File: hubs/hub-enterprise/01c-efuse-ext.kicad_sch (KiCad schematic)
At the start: 12 parts, among them J103 PJ-002AH, U103 TPS25940LRVCR

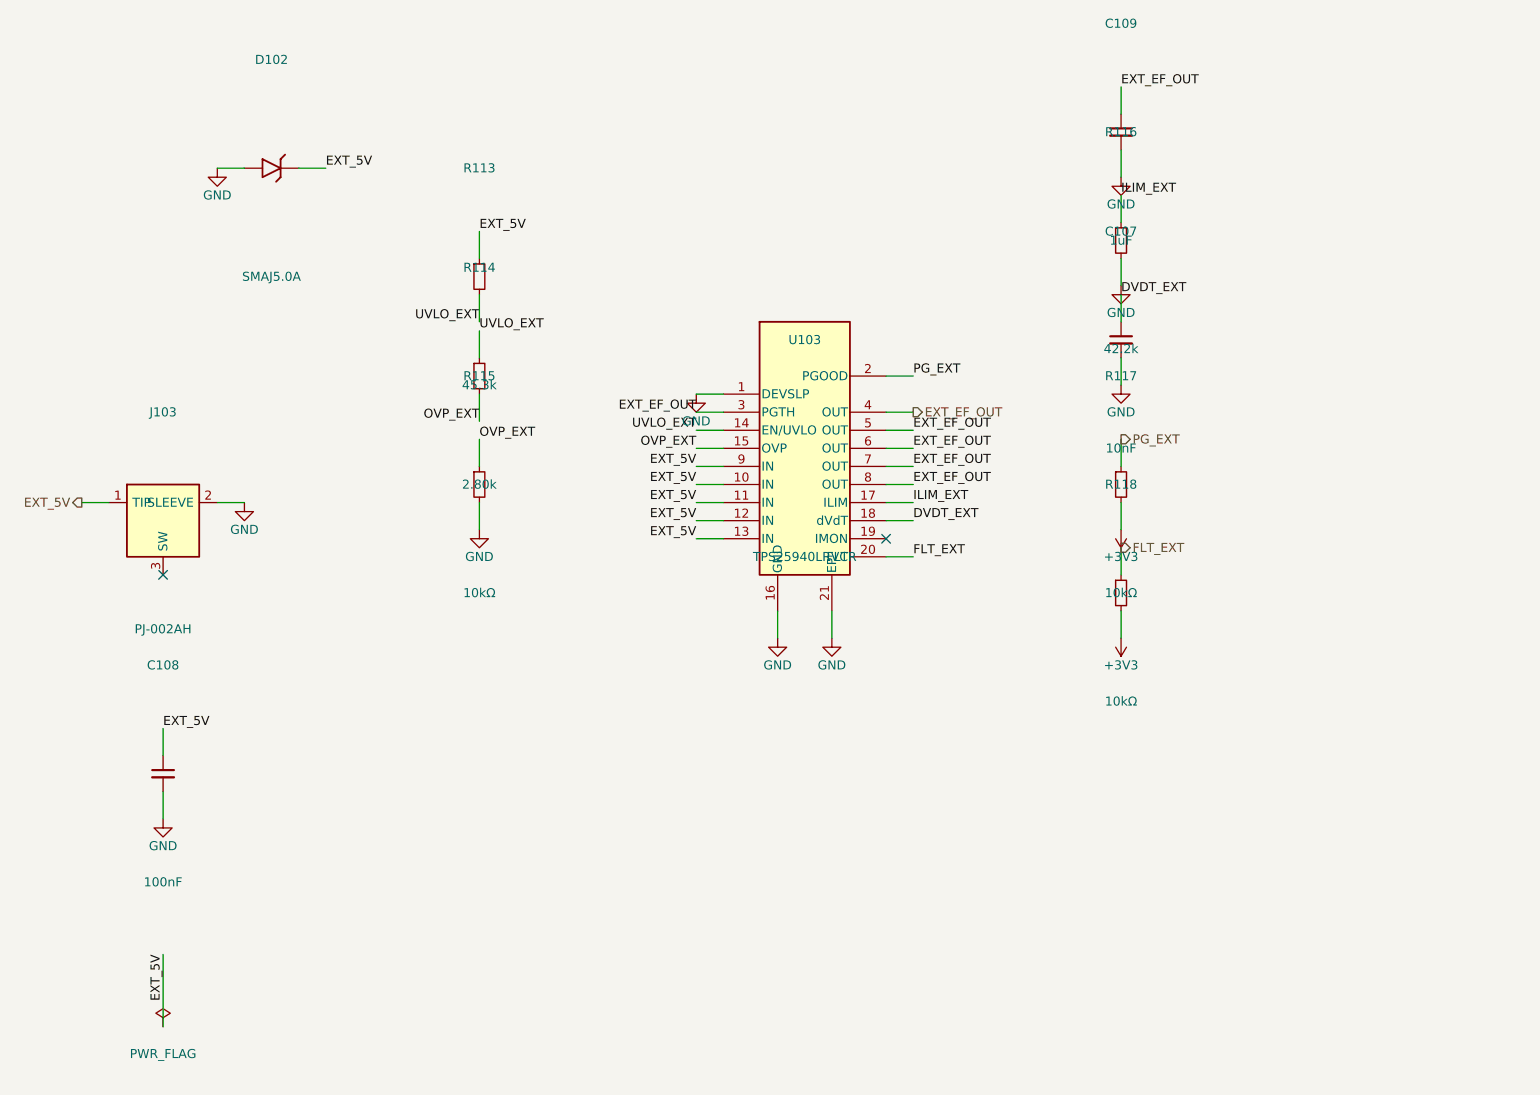
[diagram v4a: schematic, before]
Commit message: T1 composition pass: centered sheets, wired decouplers, drawn structure
Owner ask applied across the generated ENT hub sheets: content is
centered on the page (leaves moved A3->A4), decoupling caps sit at
their owner IC and connect by real drawn Manhattan wires instead of
floating label aliases, divider chains / pull-ups / ILIM parts are
drawn structure, and the thin parent is a genuine flow diagram --
per-side sheet pins, real eFuse->cascade fan-in wires on collision-free
lanes, EXT_5V routed to rail-sense with a junctioned tap, sheet-pin
names rendered inside their boxes (the owner-visible garble was the
justify convention, measured and fixed).

Mechanisms: build_leaf consumes a composed layout (wires, hier_at
overrides, decoupler rails, per-part text side) with a content-bbox
centering pass, geometry-aware Ref/Value placement, auto-junctions,
and away-side power stamps; per-leaf compose_*() in the generator (one
eFuse template drives 01a/b/c; 01e runs place_decouplers/
wire_decouplers verbatim); nudge_texts as the finishing pass. The
parent's box geometry is grid-aligned so sheet pins sit both on-edge
and on-grid -- the entire endpoint_off_grid ERC class is gone (19->0).

Real T1 bug found via render iteration: property bboxes must be
computed at the RENDERED angle (symbol rotation + field angle) -- a
rot-90 inductor's value was bboxed vertical, false-collided, and got
nudged 40mm away. Fixed in cec_sch_layout with RotatedFieldBBoxTest
(12/12).

Gates, all verified independently: netlist identity 0 missing/0 extra
(59 components, 46 groups, checker exit 0); ERC 4 benign classes only,
no annotation warning; overlaps 0 on all 8 generated sheets (was 45
pairs); lint ERROR 0 (was 38), 15 documented SL-04 WARNs. Charter T1
row: integration DONE; gates 5/6 ADOPTED into the per-sheet protocol.

Co-Authored-By: Claude Fable 5 <noreply@anthropic.com>
Claude-Session: https://claude.ai/code/session_011q5bmwF5BFtSf8Ft5vT1DZ
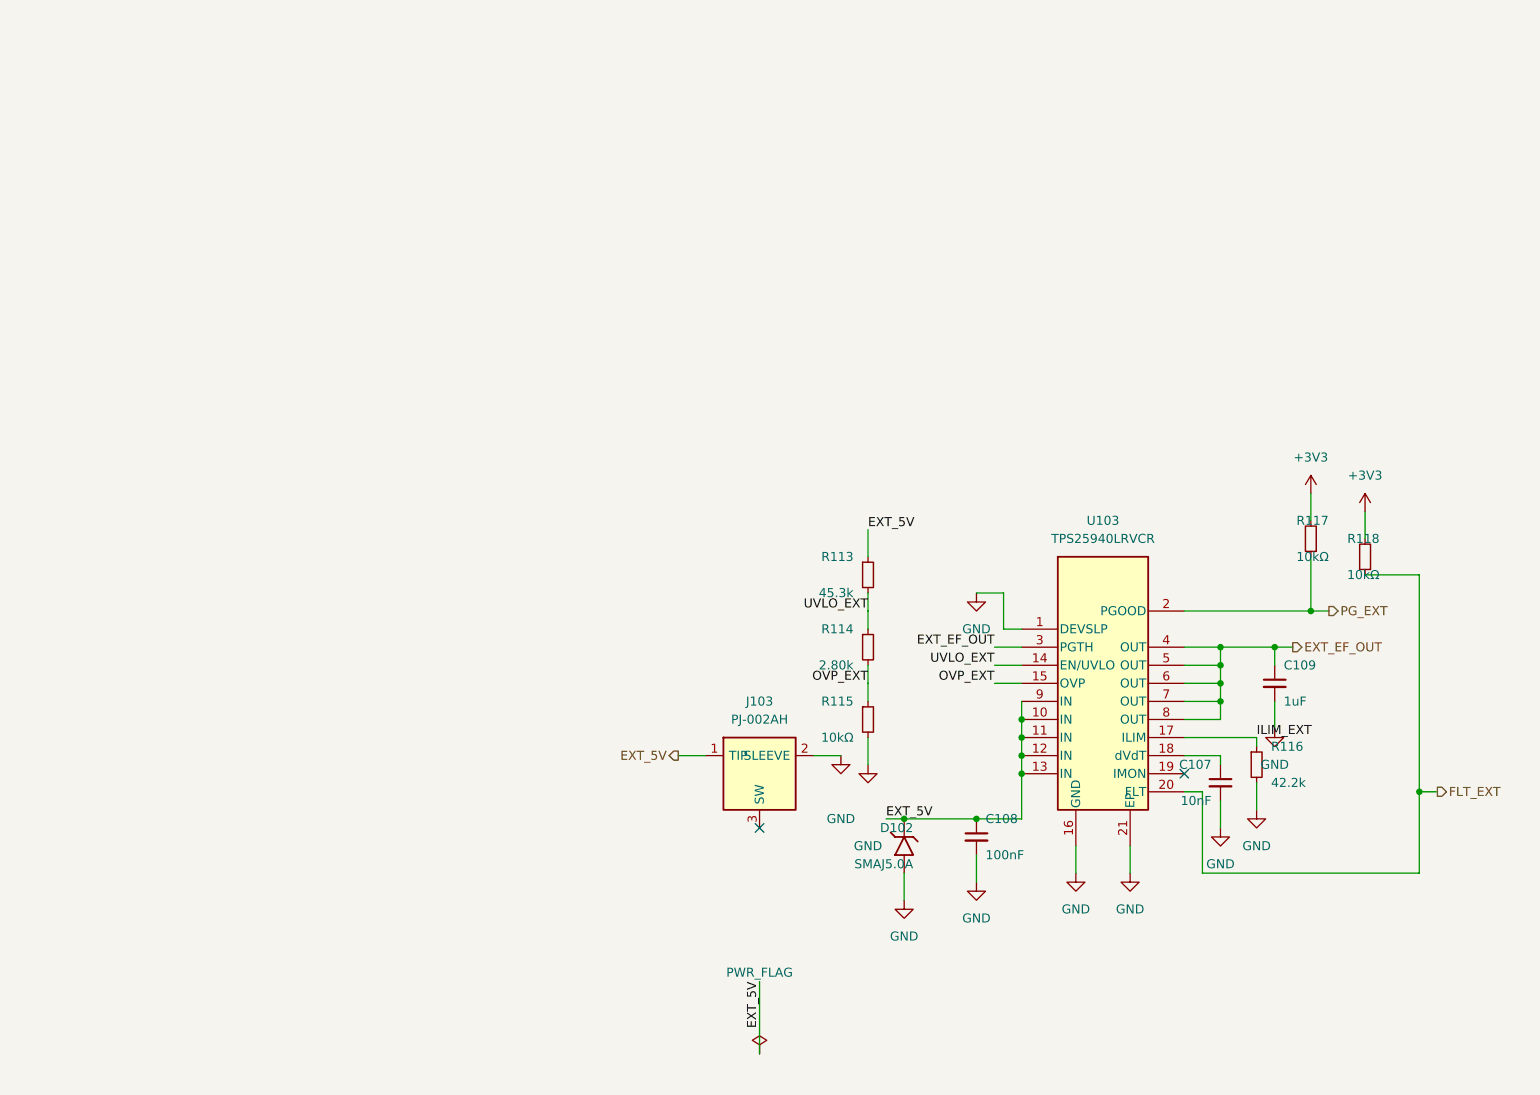
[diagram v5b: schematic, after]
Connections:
- net DVDT_EXT: no longer names the net of C107.1, U103.18 (dVdT)

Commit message: WIP snapshot: composition agent hub regeneration in flight (durability)
Co-Authored-By: Claude Fable 5 <noreply@anthropic.com>
Claude-Session: https://claude.ai/code/session_011q5bmwF5BFtSf8Ft5vT1DZ
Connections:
- net EXT_5V is gone; now on net GND: C108.1, D102.2 (K), J103.1 (TIP), R113.1, U103.10 (IN), U103.11 (IN), U103.12 (IN), U103.13 (IN), U103.9 (IN)
- net FLT_EXT: now also R118.2
- net PG_EXT: now also R117.2
- removed net +3V3: R117.2, R118.2
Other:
- note added: "EXT eFuse front + TVS (TPS25940, ILIM 42.2k -> 2.08A typ, SMAJ5.0A + PJ-002AH)"
- note added: "SMAJ5.0A input TVS populated on EXT only (mirrors the DETECT-pin philosophy); PJ-002AH barrel jack per BOM-D"
- note added: "UVLO/OVLO divider 45.3k/2.80k/10k -> 4.49V UV / 5.75V OV; ILIM 42.2k -> 2.08A typ (bom-d-power.md)"

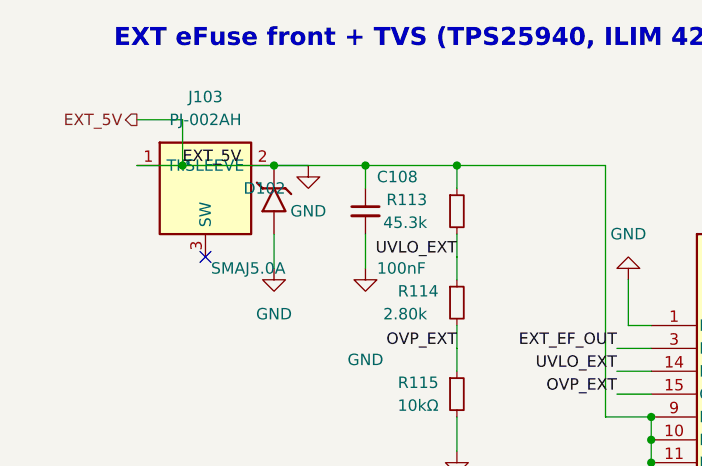
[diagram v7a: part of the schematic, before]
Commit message: WIP snapshot: composition agent iterating (durability)
Co-Authored-By: Claude Fable 5 <noreply@anthropic.com>
Claude-Session: https://claude.ai/code/session_011q5bmwF5BFtSf8Ft5vT1DZ
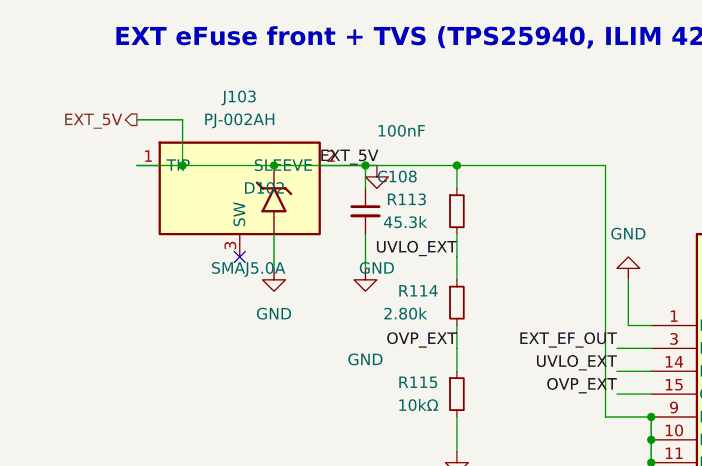
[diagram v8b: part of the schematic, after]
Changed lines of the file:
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@@
 	(symbol
 		(lib_id "cec-ent-hub-local:PJ-002AH")
-		(at 64.77 69.85 0)
-		(unit 1)
-		(exclude_from_sim no)
-		(in_bom yes)
-		(on_board yes)
-		(dnp no)
-		(fields_autoplaced yes)
-		(property "Reference" "J103" (at 64.77 59.69 0) (effects (font (size 1.27 1.27))))
-		(property "Value" "PJ-002AH" (at 64.77 62.23 0) (effects (font (size 1.27 1.27))))
-		(property "Footprint" "cec-ent-hub-local:PJ-002AH_THT_RA" (at 64.77 69.85 0) (effects (font (size 1.27 1.27)) (hide yes)))
-		(property "Datasheet" "https://www.sameskydevices.com/product/resource/pj-002ah.pdf" (at 64.77 69.85 0) (effects (font (size 1.27 1.27)) (hide yes)))
-		(property "Manufacturer" "Same Sky (CUI Devices)" (at 64.77 69.85 0) (effects (font (size 1.27 1.27)) (hide yes)))
-		(property "MPN" "PJ-002AH" (at 64.77 69.85 0) (effects (font (size 1.27 1.27)) (hide yes)))
-		(property "Description" "EXT rear-bracket power-in, 5.5/2.1mm barrel jack (BOM-D recommendation over a keyed JST -- 'any generic 5V adapter should work'; owner nod still open, see Open Items). No LCSC C-number (DigiKey #408446 only), per BOM-D." (at 64.77 69.85 0) (effects (font (size 1.27 1.27)) (hide yes)))
+		(at 68.58 69.85 0)
+		(unit 1)
+		(exclude_from_sim no)
+		(in_bom yes)
+		(on_board yes)
+		(dnp no)
+		(fields_autoplaced yes)
+		(property "Reference" "J103" (at 68.58 59.69 0) (effects (font (size 1.27 1.27))))
+		(property "Value" "PJ-002AH" (at 68.58 62.23 0) (effects (font (size 1.27 1.27))))
+		(property "Footprint" "cec-ent-hub-local:PJ-002AH_THT_RA" (at 68.58 69.85 0) (effects (font (size 1.27 1.27)) (hide yes)))
+		(property "Datasheet" "https://www.sameskydevices.com/product/resource/pj-002ah.pdf" (at 68.58 69.85 0) (effects (font (size 1.27 1.27)) (hide yes)))
+		(property "Manufacturer" "Same Sky (CUI Devices)" (at 68.58 69.85 0) (effects (font (size 1.27 1.27)) (hide yes)))
+		(property "MPN" "PJ-002AH" (at 68.58 69.85 0) (effects (font (size 1.27 1.27)) (hide yes)))
+		(property "Description" "EXT rear-bracket power-in, 5.5/2.1mm barrel jack (BOM-D recommendation over a keyed JST -- 'any generic 5V adapter should work'; owner nod still open, see Open Items). No LCSC C-number (DigiKey #408446 only), per BOM-D." (at 68.58 69.85 0) (effects (font (size 1.27 1.27)) (hide yes)))
 		(pin "1")
 		(pin "2")
@@
 		(fields_autoplaced yes)
 		(property "Reference" "C108" (at 83.82 68.58 0) (effects (font (size 1.27 1.27)) (justify left)))
-		(property "Value" "100nF" (at 83.82 78.74 0) (effects (font (size 1.27 1.27)) (justify left)))
+		(property "Value" "100nF" (at 83.82 63.5 0) (effects (font (size 1.27 1.27)) (justify left)))
 		(property "Footprint" "cec-Capacitor_SMD:C_0402_1005Metric" (at 82.55 72.39 0) (effects (font (size 1.27 1.27)) (hide yes)))
 		(property "Datasheet" "" (at 82.55 72.39 0) (effects (font (size 1.27 1.27)) (hide yes)))
@@
 	(wire (pts (xy 62.23 67.31) (xy 72.39 67.31))
 		(stroke (width 0) (type default)))
-	(wire (pts (xy 72.39 67.31) (xy 82.55 67.31))
+	(wire (pts (xy 72.39 67.31) (xy 77.47 67.31))
+		(stroke (width 0) (type default)))
+	(wire (pts (xy 77.47 67.31) (xy 82.55 67.31))
 		(stroke (width 0) (type default)))
 	(wire (pts (xy 82.55 67.31) (xy 92.71 67.31))
@@
 	(wire (pts (xy 160.02 107.95) (xy 162.56 107.95))
 		(stroke (width 0) (type default)))
-	(wire (pts (xy 72.39 67.31) (xy 76.2 67.31))
+	(wire (pts (xy 80.01 67.31) (xy 83.82 67.31))
 		(stroke (width 0) (type default)))
 	(wire (pts (xy 72.39 74.93) (xy 72.39 78.74))
@@
 	(junction (at 160.02 82.55) (diameter 0) (color 0 0 0 0))
 	(junction (at 160.02 107.95) (diameter 0) (color 0 0 0 0))
-	(label "EXT_5V" (at 62.23 67.31 0) (effects (font (size 1.27 1.27)) (justify left bottom)))
+	(label "EXT_5V" (at 77.47 67.31 0) (effects (font (size 1.27 1.27)) (justify left bottom)))
 	(label "UVLO_EXT" (at 92.71 77.47 180) (effects (font (size 1.27 1.27)) (justify right bottom)))
 	(label "OVP_EXT" (at 92.71 87.63 180) (effects (font (size 1.27 1.27)) (justify right bottom)))
@@
 	(symbol
 		(lib_id "cec-power:GND")
-		(at 76.2 67.31 0)
-		(unit 1)
-		(exclude_from_sim no)
-		(in_bom yes)
-		(on_board yes)
-		(dnp no)
-		(property "Reference" "#PWR303" (at 76.2 64.77 0) (effects (font (size 1.27 1.27)) (hide yes)))
-		(property "Value" "GND" (at 76.2 72.39 0) (effects (font (size 1.27 1.27))))
+		(at 83.82 67.31 0)
+		(unit 1)
+		(exclude_from_sim no)
+		(in_bom yes)
+		(on_board yes)
+		(dnp no)
+		(property "Reference" "#PWR303" (at 83.82 64.77 0) (effects (font (size 1.27 1.27)) (hide yes)))
+		(property "Value" "GND" (at 83.82 78.74 0) (effects (font (size 1.27 1.27))))
 		(pin "1")
 		(instances
@@
 		)
 	)
-	(no_connect (at 64.77 77.47))
+	(no_connect (at 68.58 77.47))
 	(no_connect (at 142.24 105.41))
 	(sheet_instances
